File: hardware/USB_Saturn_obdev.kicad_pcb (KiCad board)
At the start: 2 copper layers, 79.3 x 47.9 mm, 22 parts, among them CON1 AVR-ISP-6, J1 USB_B, J2 CONN_01X09, J3 CONN_01X09, U1 ATMEGA328-PU, X1 12M

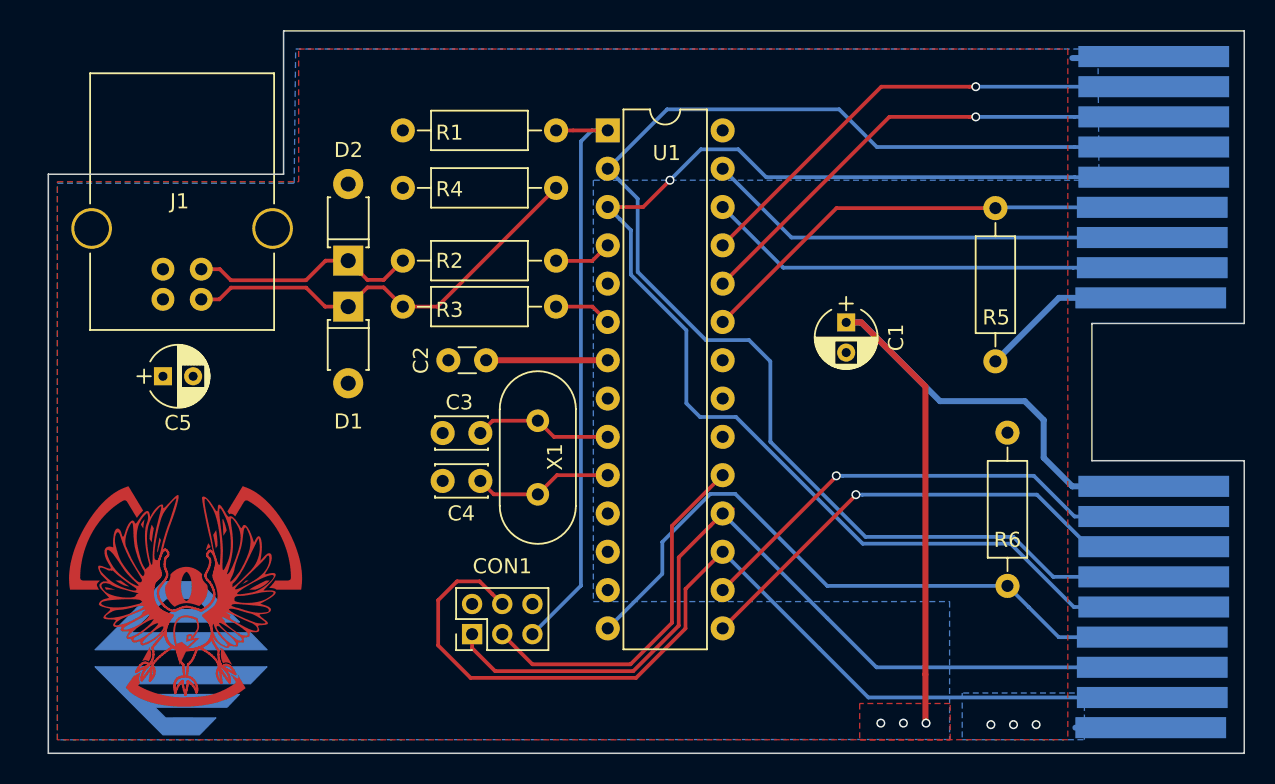
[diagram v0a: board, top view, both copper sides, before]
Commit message: Added backup library
Changed logos
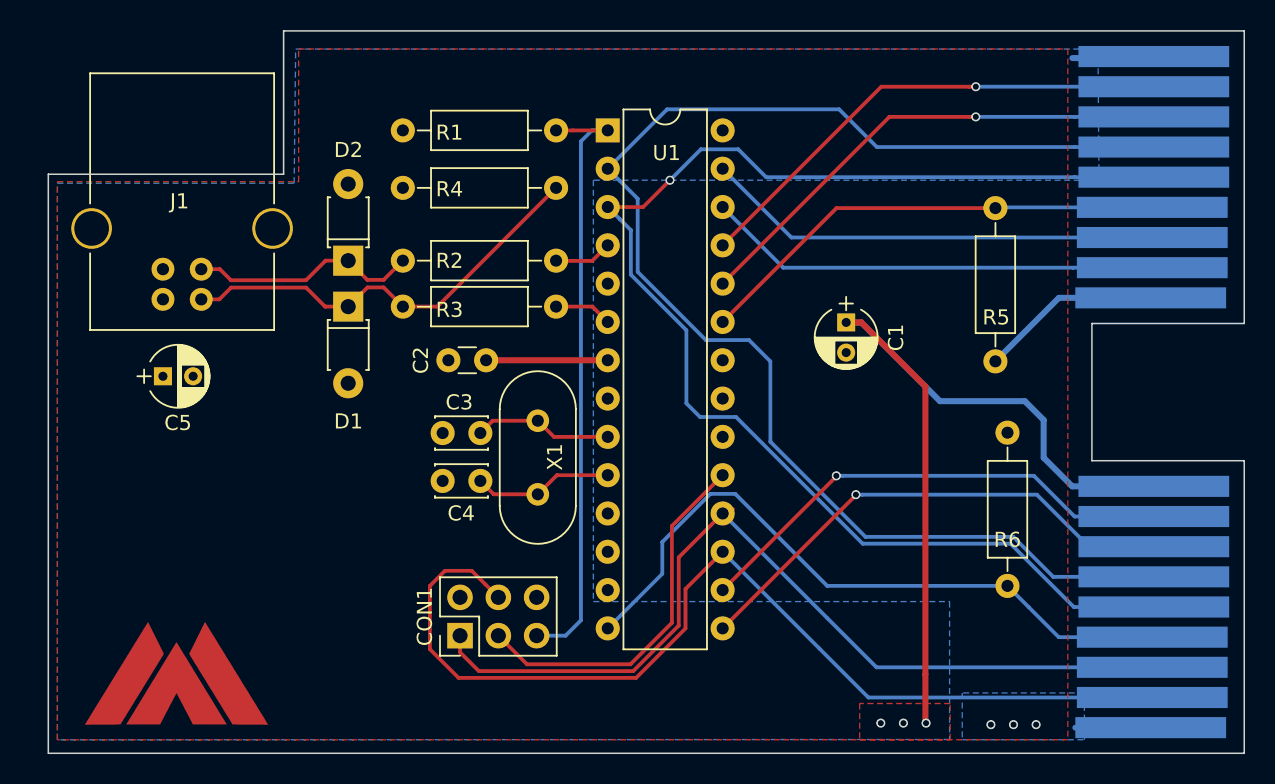
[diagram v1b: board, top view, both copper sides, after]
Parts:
- removed the svg2mod at (102.5, 116.5)
- removed the svg2mod at (102.2, 120.6)
- added logo_MA2: G***, logos:logo_MA2, F.Cu at (101.9, 121.6)
- CON1: footprint Pin_Headers:Pin_Header_Straight_2x03_Pitch2.00mm -> Pin_Headers:Pin_Header_Straight_2x03_Pitch2.54mm
- moved svg2mod 10.9 mm to (101.9, 120.3)
- moved CON1 0.81 mm to (120.7, 119.1)
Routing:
- net /D2_1: track 65.6 -> 68.5 mm
- net /!RESET: track 39.5 -> 40.6 mm
- net /D3_1: track 58.7 -> 59.5 mm

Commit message: Kicad format changes
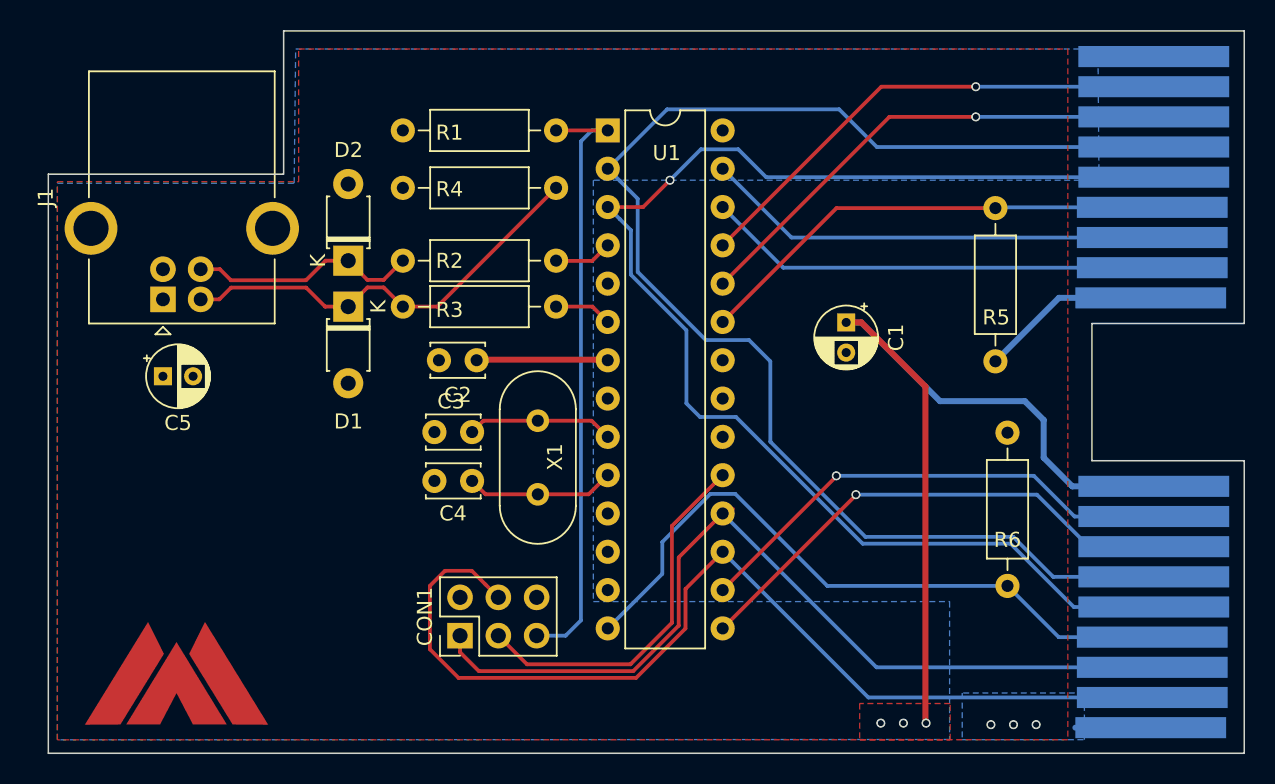
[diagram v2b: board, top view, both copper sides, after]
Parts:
- C1, C5: footprint Capacitors_THT:CP_Radial_D4.0mm_P2.00mm -> Capacitor_THT:CP_Radial_D4.0mm_P2.00mm
- C2: footprint Capacitors_THT:C_Disc_D3.0mm_W1.6mm_P2.50mm -> Capacitor_THT:C_Disc_D3.4mm_W2.1mm_P2.50mm
- C3, C4: footprint Capacitors_THT:C_Disc_D3.4mm_W2.1mm_P2.50mm -> Capacitor_THT:C_Disc_D3.4mm_W2.1mm_P2.50mm
- CON1: footprint Pin_Headers:Pin_Header_Straight_2x03_Pitch2.54mm -> Connector_PinHeader_2.54mm:PinHeader_2x03_P2.54mm_Vertical
- D1, D2: footprint Diodes_THT:D_T-1_P5.08mm_Horizontal -> Diode_THT:D_T-1_P5.08mm_Horizontal
- J1: footprint Connectors:USB_B -> Connector_USB:USB_B_OST_USB-B1HSxx_Horizontal
- R1, R2, R3, R4, R5, R6: footprint Resistors_THT:R_Axial_DIN0207_L6.3mm_D2.5mm_P10.16mm_Horizontal -> Resistor_THT:R_Axial_DIN0207_L6.3mm_D2.5mm_P10.16mm_Horizontal
- U1: footprint Housings_DIP:DIP-28_W7.62mm -> Package_DIP:DIP-28_W7.62mm
- X1: footprint Crystals:Crystal_HC49-4H_Vertical -> Crystal:Crystal_HC49-4H_Vertical
- moved C2 0.63 mm to (121.8, 100.8)
- moved C3 0.55 mm to (119.0, 105.6)
- moved C4 0.55 mm to (119.0, 108.8)
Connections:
- U1 pad 11: Net-(U1-Pad11) -> (no net)
- U1 pad 12: Net-(U1-Pad12) -> (no net)
- U1 pad 13: Net-(U1-Pad13) -> (no net)
- U1 pad 20: Net-(U1-Pad20) -> (no net)
- U1 pad 21: Net-(U1-Pad21) -> (no net)
- U1 pad 28: Net-(U1-Pad28) -> (no net)
- U1 pad 5: Net-(U1-Pad5) -> (no net)
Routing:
- net +5V: track 69.1 -> 64.4 mm
- net Net-(C4-Pad2): track 9.34 -> 9.89 mm
- net Net-(C3-Pad2): track 9.23 -> 9.75 mm
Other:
- net class pwr: clearance 0.3 -> 0.2
